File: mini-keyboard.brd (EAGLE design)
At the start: 100 x 80 mm, 28 parts, among them P1 500, P2 500, P3 500, P4 500, P5 500, P6 500, P7 500, P8 500, U1 SN74HC148DIP, U2 CD4512BE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

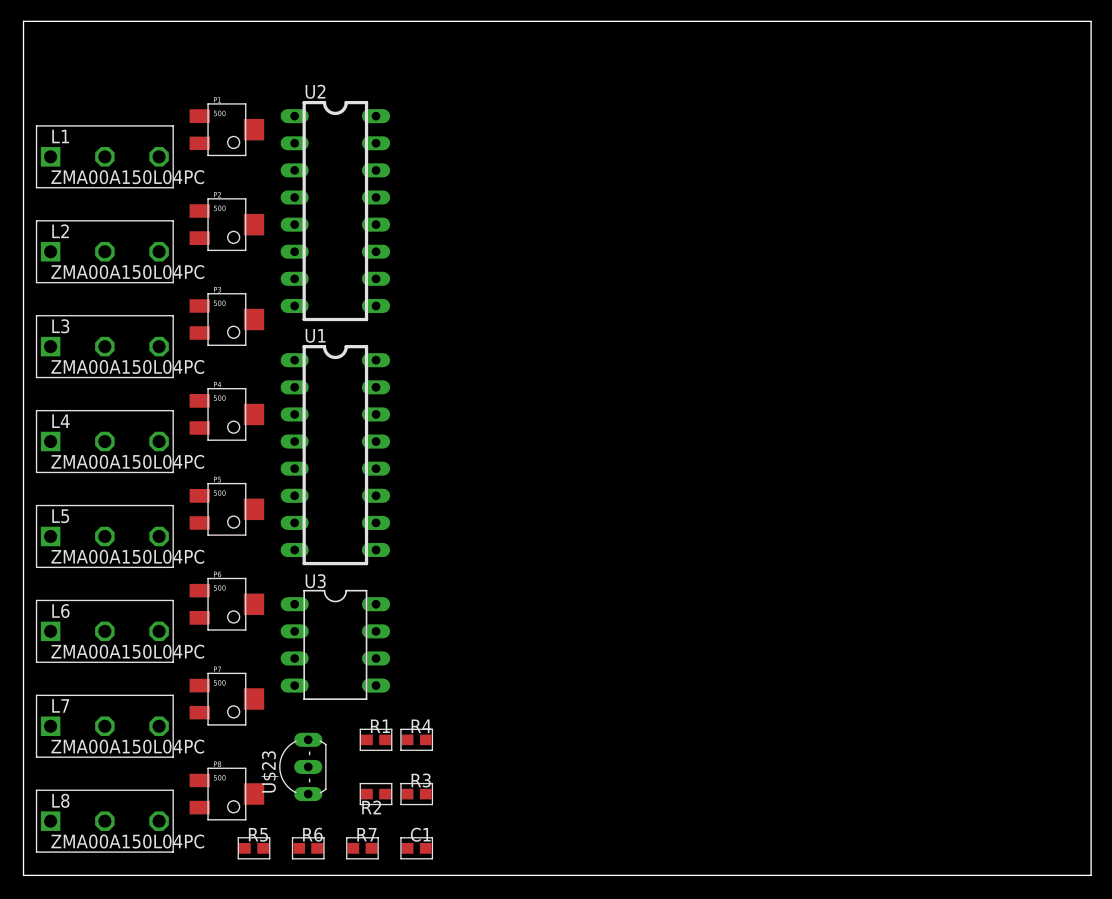
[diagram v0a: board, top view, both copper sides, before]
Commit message: Finished board, added pwr connector, LED, and audio connector for 3.5mm stereo
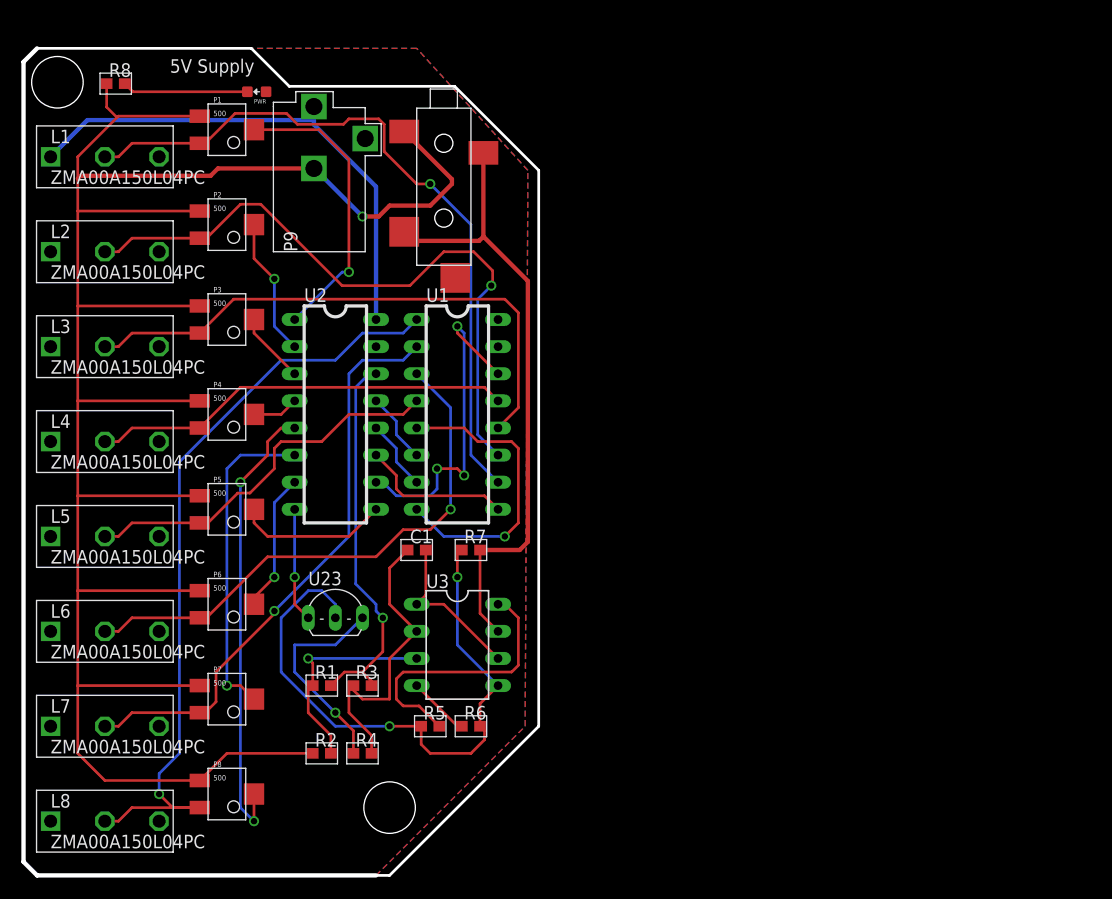
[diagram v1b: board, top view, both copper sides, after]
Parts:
- removed U$23: 2N7000-G, Transistors:TO92-CBE
- added J1: SJ-3523-SMT, audio-connectors:SJ-352X-SMT
- added P9: (no value), PWR-Connectors:BARREL-SPFUN-BRBRD
- added PWR: LED-STD, LED:0603
- added R8: 1k, RCL:0603
- added U23: 2N7000-G, Transistors:TO92-CBE
- moved R7 29.7 mm to (41.9, 30.5)
- moved C1 27.9 mm to (36.8, 30.5)
- moved R5 20.1 mm to (38.1, 14.0)
- moved R6 19.0 mm to (41.9, 14.0)
- moved U2 19.0 mm to (29.2, 43.2)
- moved U1 12.0 mm to (40.6, 43.2)
- moved U3 11.4 mm to (40.6, 21.6)
- moved R3 11.4 mm to (31.8, 17.8)
- moved R1 7.18 mm to (27.9, 17.8)
- moved R2 6.35 mm to (27.9, 11.4), turned to 0 degrees
- moved R4 5.24 mm to (31.8, 11.4)
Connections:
- new net N$3: U1.14, U2.10
- new net N$7: PWR.OUT, R8.2
- net 5V: now also P9.1, PWR.IN; no longer U1.15
- net GND: now also J1.1, P9.2, R8.1, U23.1; no longer U$23.1, U1.14, U2.10
- net N$1: now also U23.3; no longer U$23.3
- net N$5: now also J1.2, J1.3
- net N$6: now also U23.2; no longer U$23.2
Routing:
- net GND: track 0.00 -> 255.4 mm, vias 0 -> 3
- net 5V: track 0.00 -> 74.3 mm
- net D4: track 0.00 -> 73.4 mm, vias 0 -> 1
- net D0: track 0.00 -> 67.4 mm, vias 0 -> 1
- net D1: track 0.00 -> 62.0 mm, vias 0 -> 1
- net N$5: track 0.00 -> 59.2 mm
- net N$6: track 0.00 -> 57.4 mm, vias 0 -> 2
- net D5: track 0.00 -> 54.8 mm, vias 0 -> 1
- net D2: track 0.00 -> 52.7 mm
- net D6: track 0.00 -> 51.1 mm, vias 0 -> 1
- net S4: track 0.00 -> 42.7 mm, vias 0 -> 2
- net D3: track 0.00 -> 39.5 mm
- net N$2: track 0.00 -> 36.1 mm, vias 0 -> 1
- net D7: track 0.00 -> 35.6 mm
- net N$3: track 0.00 -> 31.5 mm, vias 0 -> 3
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- added copper zone on layer 1, net 5V
- added copper zone on layer 16, net GND
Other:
- board size 100 x 80 mm -> 48.3 x 77.5 mm
- board text added: "5V Supply"
- board text added: "By Neeraj Gandhi"
- board text added: "Mini-Keyboard V1"
